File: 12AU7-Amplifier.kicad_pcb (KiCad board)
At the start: 2 copper layers, 100 x 75 mm, 36 parts, among them CON1 AudioIn, CON2 AudioOut, J1 Barrel_Jack, Q1 IRF510, Q2 IRF510, SW1 SW_SPST, U1 12AU7, U2 LM317, U3 LM317

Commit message: Add ground plane and trace routing
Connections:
- J1 pad 3: (no net) -> GND
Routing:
- net +12V: track 0.00 -> 199.7 mm
- net Net-(C6-Pad2): track 0.00 -> 82.8 mm
- net Net-(C3-Pad1): track 0.00 -> 63.7 mm
- net Net-(J1-Pad1): track 0.00 -> 60.0 mm
- net Net-(Q1-Pad1): track 0.00 -> 57.4 mm
- net Net-(Q2-Pad1): track 0.00 -> 52.9 mm
- net Net-(CON1-Pad3): track 0.00 -> 49.6 mm
- net Net-(C4-Pad1): track 0.00 -> 46.3 mm
- net Net-(C1-Pad2): track 0.00 -> 45.4 mm
- net Net-(CON1-Pad2): track 0.00 -> 38.9 mm
- net Net-(C1-Pad1): track 0.00 -> 38.2 mm
- net Net-(C2-Pad2): track 0.00 -> 38.1 mm
- net Net-(C5-Pad1): track 0.00 -> 35.6 mm
- net Net-(C6-Pad1): track 0.00 -> 34.6 mm
- net Net-(C5-Pad2): track 0.00 -> 30.2 mm
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- added copper zone on B.Cu, net GND
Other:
- net class Default: clearance 0.2 -> 0.5; trace_width 0.25 -> 0.5
- rule trace_clearance: 0.2 -> 0.5
- rule trace_min: 0.2 -> 0.25
- board text added: "12AU7 Headphone Amplifier"
- board text added: "=^.^="
- board text added: "Aaron & Ryan Shappell"

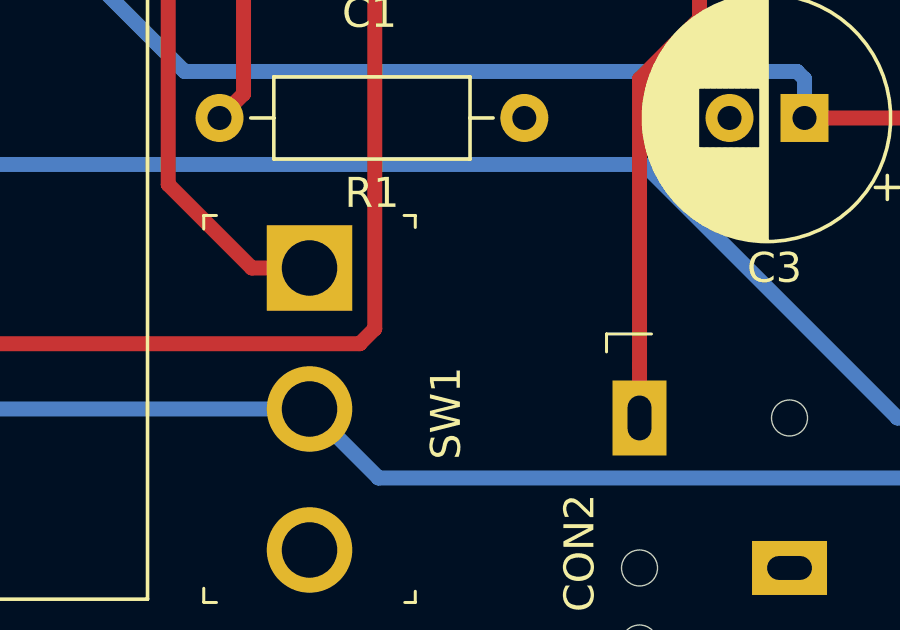
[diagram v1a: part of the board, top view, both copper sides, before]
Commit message: add smoothing capacitor
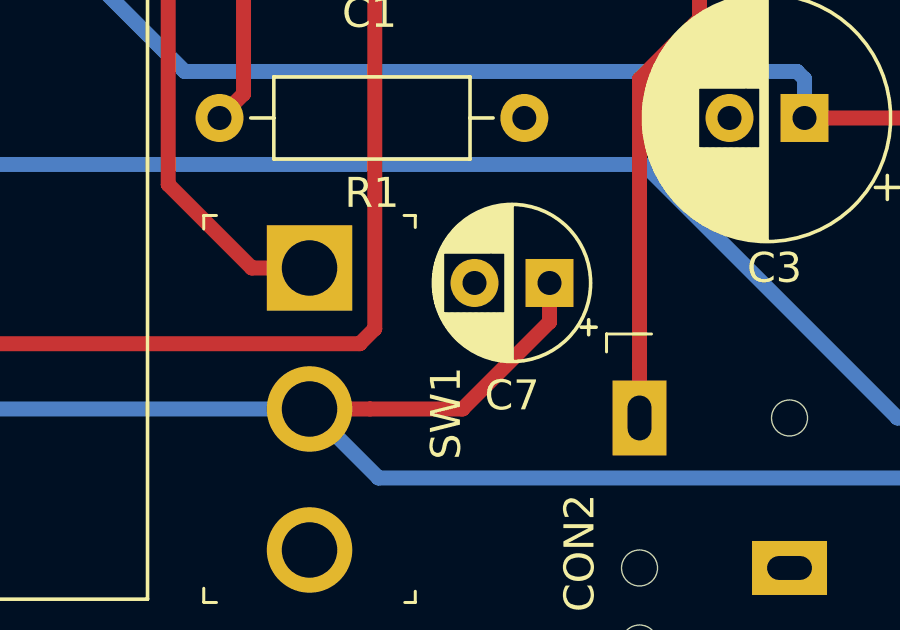
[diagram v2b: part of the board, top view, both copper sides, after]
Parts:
- added C7: 10uF, Capacitor_THT:CP_Radial_D5.0mm_P2.50mm, F.Cu at (177.0, 136.5)
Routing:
- net +12V: track 199.7 -> 210.2 mm
